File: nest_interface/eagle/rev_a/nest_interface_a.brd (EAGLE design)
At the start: 133.3 x 110.5 mm, 111 parts, among them J1 MOLEX_MICRO_USB_B_047346, J10 CONN_BLOCK_2, J11 CONN_BLOCK_2, J12 CONN_BLOCK_2, J13 CONN_BLOCK_2, J14 CONN_BLOCK_3, J15 CONN_BLOCK_3, J16 CONN_BLOCK_7, J17 CONN_BLOCK_7, J18 CONN_BLOCK_8, J19 CONN_BLOCK_8, J2 MOLEX_MICRO_USB_B_047346, J20 CONN_BLOCK_8, J21 CONN_BLOCK_8, J5 PJ-036A-SMT, J6 CONN_BLOCK_2, J7 CONN_BLOCK_2, J8 CONN_BLOCK_2, J9 CONN_BLOCK_2, U1 EPIC-CORE_A, U2 MSP430F1611IPM, U3 FT232RL, U4 FT232RL, U5 MPC1825, U6 TC1262, U7 PCA9575, U8 PCA9575, Y1 FC-135_32.768KA-A3

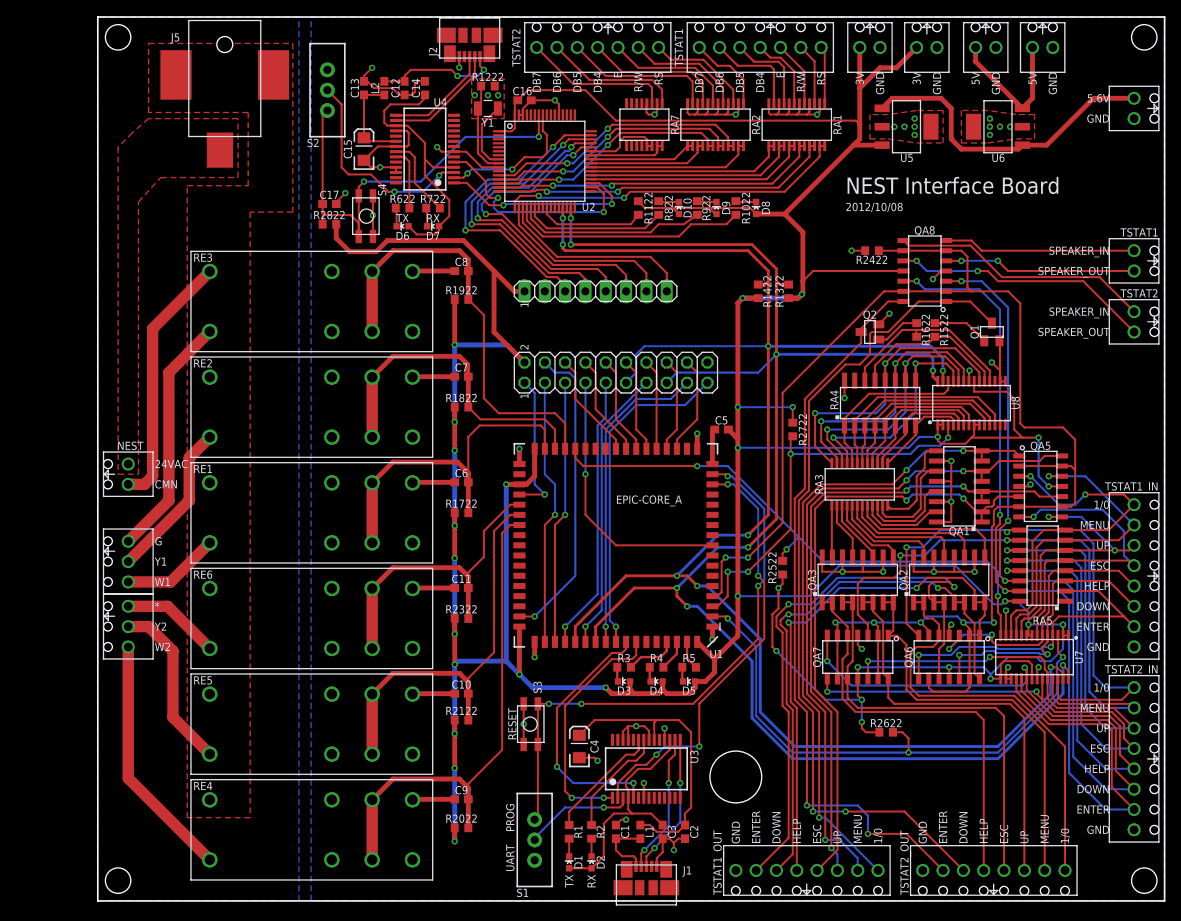
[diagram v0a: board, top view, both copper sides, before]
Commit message: added decoupling caps, bom
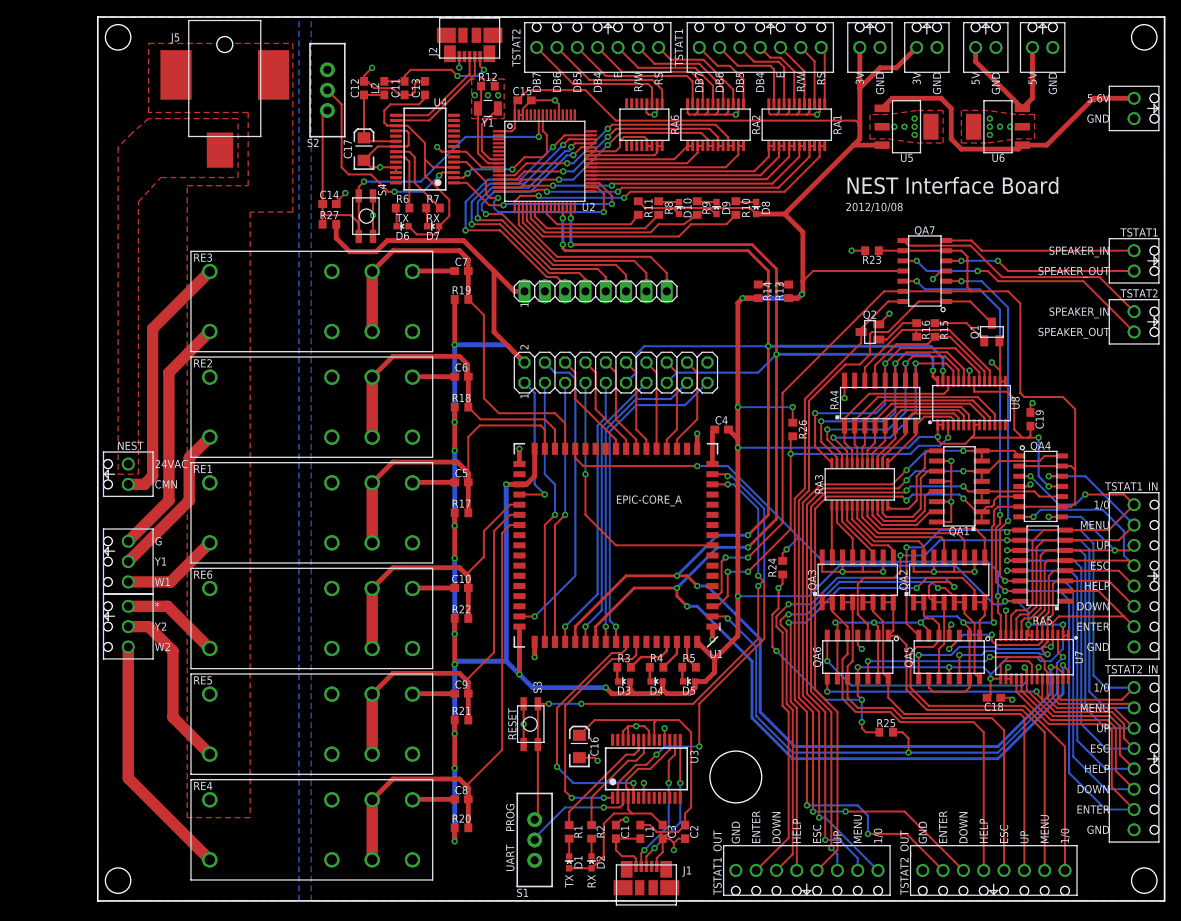
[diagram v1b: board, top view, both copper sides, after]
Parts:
- removed QA8: ALD1107, nest_interface:SOIC-14
- added C18, C19: 0.1u, rcl:C0603
- added QA4: ALD1107, nest_interface:SOIC-14
- C10, C11, C6, C7, C8, C9: value .1u -> 0.1u
- C15: value 10u -> 1u; device SparkFun:EIA3216 -> rcl:C0603
- C16: value 1u -> 10u; device rcl:C0603 -> SparkFun:EIA3216
- C17: value 0.1u -> 10u; device rcl:C0603 -> SparkFun:EIA3216
- C4: value 10u -> 0.1u; device SparkFun:EIA3216 -> rcl:C0603
- moved C16 81.1 mm to (60.2, 19.3), turned to 90 degrees
- moved C8 66.0 mm to (45.5, 12.7)
- moved C11 62.9 mm to (38.4, 101.6), turned to 270 degrees
- moved QA7 49.0 mm to (103.4, 78.7), turned to 90 degrees
- moved C4 43.4 mm to (78.0, 58.9), turned to 180 degrees
- moved C5 33.2 mm to (45.5, 52.3)
- moved QA5 24.2 mm to (106.4, 30.5), turned to 180 degrees
- moved C15 21.0 mm to (53.3, 100.1), turned to 0 degrees
- moved C14 18.8 mm to (29.0, 87.1), turned to 0 degrees
- moved C9 13.2 mm to (45.5, 25.9)
- moved C10 13.2 mm to (45.5, 39.1)
- moved C6 13.2 mm to (45.5, 65.5)
- moved C7 13.2 mm to (45.5, 78.7)
- moved QA6 11.4 mm to (95.0, 30.5)
- moved C17 8.10 mm to (33.3, 94.0), turned to 90 degrees
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- renumbered JP1 to J4, R1022 to R10, R1122 to R11, R1222 to R12, R1322 to R13, R1422 to R14, R1522 to R15, R1622 to R16, R1722 to R17, R1822 to R18, R1922 to R19, R2022 to R20, R2122 to R21, R2322 to R22, R2422 to R23, R2522 to R24, R2622 to R25, R2722 to R26, R2822 to R27, R622 to R6, R722 to R7, R822 to R8, R922 to R9, RA7 to RA6
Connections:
- net #KEYPAD_ENABLE: now also QA4.13, QA4.2, QA4.6, QA4.9; no longer QA8.13, QA8.2, QA8.6, QA8.9
- net COOLING1_PIN: now also C6.1; no longer C7.1
- net COOLING2_PIN: now also C9.1; no longer C10.1
- net FAN_PIN: now also C7.1; no longer C8.1
- net GND: now also C15.2, C16.C, C17.C, C18.2, C19.2, C5.2, QA4.4; no longer C15.C, C16.2, C17.2, C4.C, QA8.4
- net HEATING1_PIN: now also C5.1; no longer C6.1
- net HEATING2_PIN: now also C8.1; no longer C9.1
- net N$18: now also C4.2; no longer C5.2
- net N$39: now also C11.1; no longer C12.1
- net N$43: now also C12.1, C17.A; no longer C13.1, C15.A
- net N$51: now also C13.1; no longer C14.1
- net N$6: now also C16.A; no longer C4.A
- net RST1: now also C14.1; no longer C17.1
- net STAR_PIN: now also C10.1; no longer C11.1
- net TSTAT1_DOWN_IN: now also QA5.12; no longer QA6.12
- net TSTAT1_DOWN_OUT: now also QA5.14; no longer QA6.14
- net TSTAT1_ENTER_IN: now also QA5.8; no longer QA6.8
- net TSTAT1_ENTER_OUT: now also QA5.10; no longer QA6.10
- net TSTAT1_ESC_IN: now also QA4.7; no longer QA5.7
- net TSTAT1_ESC_OUT: now also QA4.5; no longer QA5.5
- net TSTAT1_HELP_IN: now also QA5.3; no longer QA6.3
- net TSTAT1_HELP_OUT: now also QA5.1; no longer QA6.1
- net TSTAT1_MENU_IN: now also QA4.12; no longer QA5.12
- net TSTAT1_MENU_OUT: now also QA4.14; no longer QA5.14
- net TSTAT1_ON/OFF_IN: now also QA4.3; no longer QA5.3
- net TSTAT1_ON/OFF_OUT: now also QA4.1; no longer QA5.1
- net TSTAT1_SPEAKER_IN: now also QA7.7; no longer QA8.7
- net TSTAT1_SPEAKER_OUT: now also QA7.5; no longer QA8.5
- net TSTAT1_UP_IN: now also QA4.8; no longer QA5.8
- net TSTAT1_UP_OUT: now also QA4.10; no longer QA5.10
- net TSTAT2_DOWN_IN: now also QA7.3; no longer QA8.3
- net TSTAT2_DOWN_OUT: now also QA7.1; no longer QA8.1
- net TSTAT2_ENTER_IN: now also QA7.12; no longer QA8.12
- net TSTAT2_ENTER_OUT: now also QA7.14; no longer QA8.14
- net TSTAT2_ESC_IN: now also QA6.8; no longer QA7.8
- net TSTAT2_ESC_OUT: now also QA6.10; no longer QA7.10
- net TSTAT2_HELP_IN: now also QA6.7; no longer QA7.7
- net TSTAT2_HELP_OUT: now also QA6.5; no longer QA7.5
- net TSTAT2_MENU_IN: now also QA6.3; no longer QA7.3
- net TSTAT2_MENU_OUT: now also QA6.1; no longer QA7.1
- net TSTAT2_ON/OFF_IN: now also QA5.7; no longer QA6.7
- net TSTAT2_ON/OFF_OUT: now also QA5.5; no longer QA6.5
- net TSTAT2_SPEAKER_IN: now also QA7.8; no longer QA8.8
- net TSTAT2_SPEAKER_OUT: now also QA7.10; no longer QA8.10
- net TSTAT2_UP_IN: now also QA6.12; no longer QA7.12
- net TSTAT2_UP_OUT: now also QA6.14; no longer QA7.14
- net VCC: now also C15.1, C18.1, C19.1, C4.1, QA4.11; no longer C16.1, C5.1, QA8.11
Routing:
- net VCC: track 602.7 -> 606.8 mm
- net GND: track 224.8 -> 227.6 mm, vias 52 -> 54
- net TSTAT2_ESC_OUT: track 53.3 -> 52.2 mm
- net TSTAT2_HELP_OUT: track 51.9 -> 51.0 mm

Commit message: added board for keypad socket
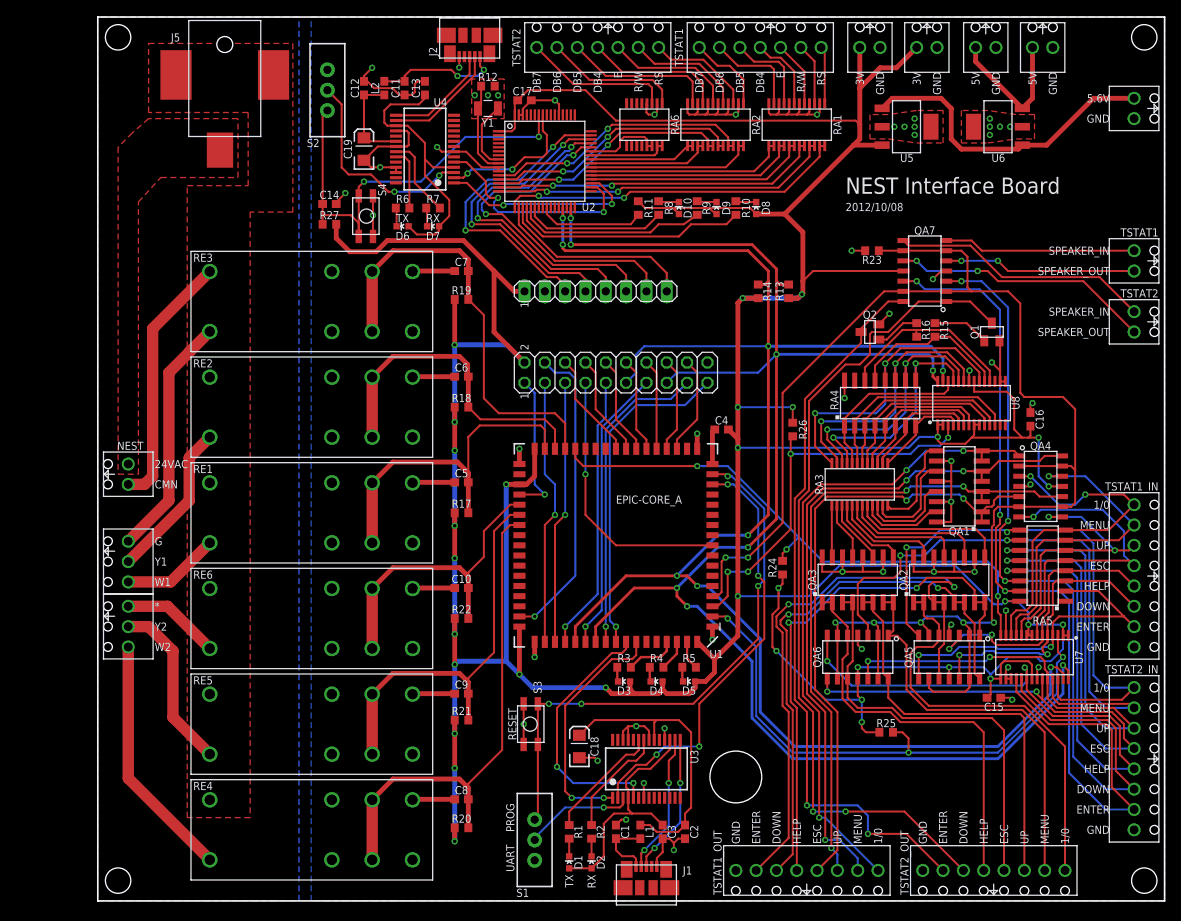
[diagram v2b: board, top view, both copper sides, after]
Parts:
- C15: value 1u -> 0.1u
- C16: value 10u -> 0.1u; device SparkFun:EIA3216 -> rcl:C0603
- C17: value 10u -> 1u; device SparkFun:EIA3216 -> rcl:C0603
- C18, C19: value 0.1u -> 10u; device rcl:C0603 -> SparkFun:EIA3216
- D1, D3, D6, D8: value (none) -> RED
- D10, D2, D5, D7: value (none) -> BLUE
- D4, D9: value (none) -> GREEN
- moved C15 95.0 mm to (112.0, 25.4)
- moved C19 89.9 mm to (33.3, 94.0)
- moved C16 69.7 mm to (116.6, 60.2)
- moved C18 52.2 mm to (60.2, 19.3), turned to 90 degrees
- moved C17 21.0 mm to (53.3, 100.1), turned to 0 degrees
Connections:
- net GND: now also C16.2, C17.2, C18.C, C19.C; no longer C16.C, C17.C, C18.2, C19.2
- net N$43: now also C19.A; no longer C17.A
- net N$6: now also C18.A; no longer C16.A
- net VCC: now also C16.1, C17.1; no longer C18.1, C19.1

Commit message: nest
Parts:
- removed J4: (no value), pinhead:1X08
- added JP1: (no value), pinhead:1X10
- added U$1: UMICH_SOLID_LARGE, nest_interface:UMICH_SOLID_350MIL
- moved S2 2.40 mm to (30.7, 102.6)
- moved C11 1.61 mm to (39.9, 102.1)
- moved C12 1.61 mm to (34.8, 102.1)
- moved C13 1.61 mm to (42.4, 102.1)
- moved L2 1.61 mm to (37.3, 102.1)
- moved C19 0.51 mm to (33.8, 94.0)
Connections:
- net P2.3 renamed LCDP_P2.3
- removed net P5.4: U2.48
- new net LCDP_P5.4: JP1.2, U2.48
- net GND: now also JP1.10; no longer J4.2
- net LCDP_MISO1: now also JP1.5; no longer J4.4
- net LCDP_MOSI1: now also JP1.6; no longer J4.5
- net LCDP_P1.6: now also JP1.8; no longer J4.7
- net LCDP_P1.7: now also JP1.9; no longer J4.8
- net LCDP_P2.4: now also JP1.3
- net LCDP_STE1: now also JP1.7; no longer J4.6
- net LCDP_UCLK1: now also JP1.4; no longer J4.3
- net VCC: now also JP1.1; no longer J4.1
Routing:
- net LCDP_P5.4: track 0.00 -> 39.8 mm, vias 0 -> 2
- net LCDP_P2.4: track 0.00 -> 13.7 mm, vias 0 -> 2
- net LCDP_MISO1: track 39.6 -> 43.8 mm
- net LCDP_MOSI1: track 40.2 -> 44.3 mm
- net LCDP_STE1: track 40.8 -> 44.7 mm
- net LCDP_P1.6: track 22.9 -> 26.6 mm
- net LCDP_P1.7: track 24.8 -> 28.5 mm
- net LCDP_UCLK1: track 38.8 -> 42.4 mm
- net N$51: track 35.0 -> 37.2 mm
- net RST1: track 55.2 -> 57.3 mm
- net N$39: track 15.9 -> 14.2 mm
- net GND: track 227.6 -> 226.6 mm
- net VCC: track 606.8 -> 607.6 mm
- net N$43: track 12.1 -> 12.8 mm
- net #KEYPAD_ENABLE: track 197.0 -> 196.2 mm
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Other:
- board text added: "24VAC SIGNALS"
- board text added: "LCD"
- board text added: "MAIN CONTROLLER"
- board text added: "VCC"

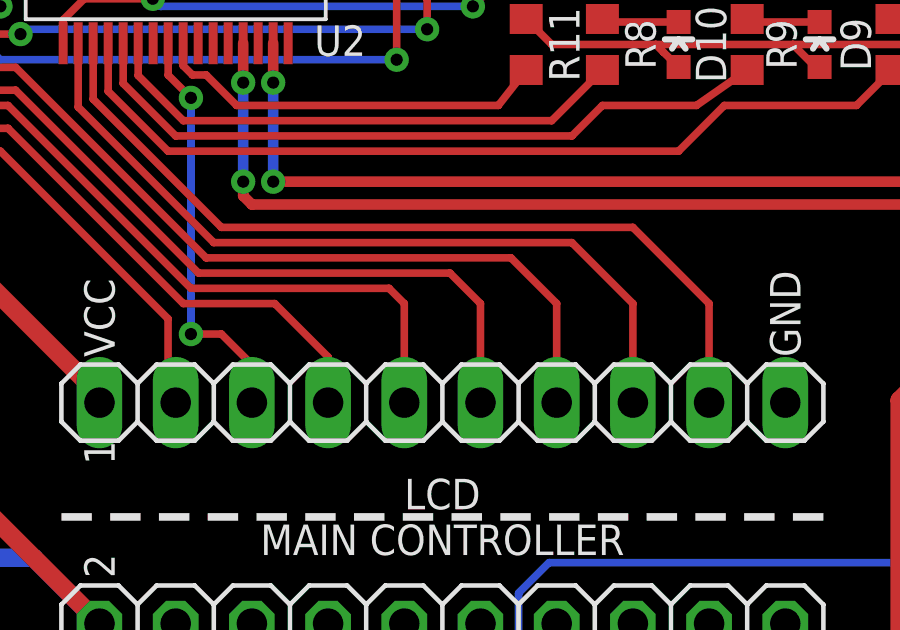
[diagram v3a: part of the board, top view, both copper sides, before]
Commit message: cleaned up two traces and started lcd code
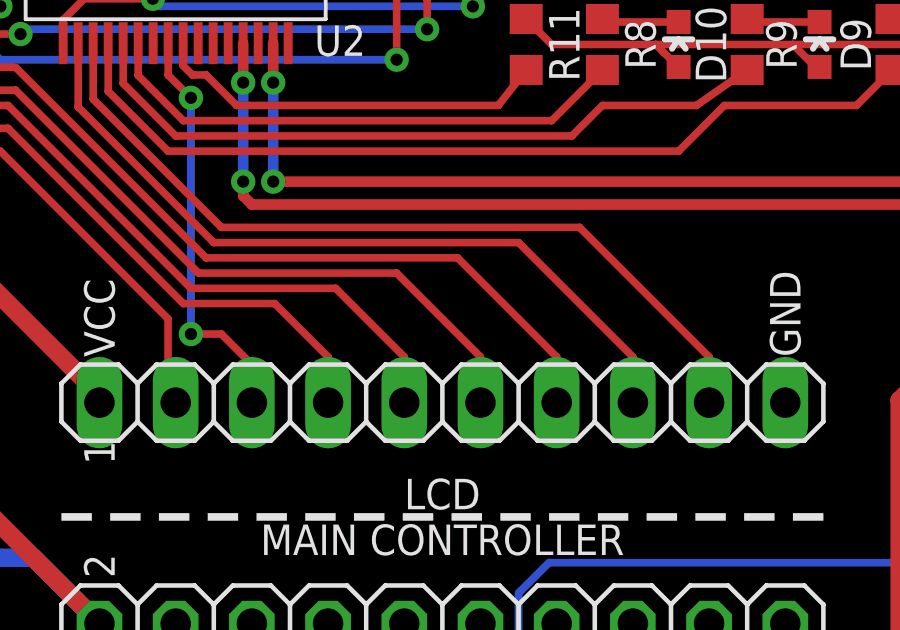
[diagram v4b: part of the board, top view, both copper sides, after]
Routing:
- net LCDP_P1.7: track 28.5 -> 27.5 mm
- net LCDP_MOSI1: track 44.3 -> 43.3 mm
- net LCDP_MISO1: track 43.8 -> 42.7 mm
- net LCDP_STE1: track 44.7 -> 43.7 mm
- net LCDP_P1.6: track 26.6 -> 25.6 mm
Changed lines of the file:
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@@
 <wire x1="50.546" y1="85.852" x2="56.896" y2="79.502" width="0.254" layer="1"/>
 <contactref element="JP1" pad="7"/>
-<wire x1="56.896" y1="79.502" x2="67.056" y2="79.502" width="0.254" layer="1"/>
-<wire x1="67.056" y1="79.502" x2="68.58" y2="77.978" width="0.254" layer="1"/>
-<wire x1="68.58" y1="77.978" x2="68.58" y2="74.676" width="0.254" layer="1"/>
+<wire x1="56.896" y1="79.502" x2="65.278" y2="79.502" width="0.254" layer="1"/>
+<wire x1="65.278" y1="79.502" x2="68.58" y2="76.2" width="0.254" layer="1"/>
+<wire x1="68.58" y1="76.2" x2="68.58" y2="74.676" width="0.254" layer="1"/>
 </signal>
 <signal name="LCDP_MOSI1">
@@
 <wire x1="59.182" y1="93.98" x2="59.182" y2="94.234" width="0.254" layer="16"/>
 <contactref element="JP1" pad="6"/>
-<wire x1="56.642" y1="78.994" x2="65.024" y2="78.994" width="0.254" layer="1"/>
-<wire x1="65.024" y1="78.994" x2="66.04" y2="77.978" width="0.254" layer="1"/>
-<wire x1="66.04" y1="77.978" x2="66.04" y2="74.676" width="0.254" layer="1"/>
+<wire x1="56.642" y1="78.994" x2="63.246" y2="78.994" width="0.254" layer="1"/>
+<wire x1="63.246" y1="78.994" x2="66.04" y2="76.2" width="0.254" layer="1"/>
+<wire x1="66.04" y1="76.2" x2="66.04" y2="74.676" width="0.254" layer="1"/>
 </signal>
 <signal name="LCDP_MISO1">
@@
 <wire x1="50.292" y1="84.582" x2="56.388" y2="78.486" width="0.254" layer="1"/>
 <contactref element="JP1" pad="5"/>
-<wire x1="56.388" y1="78.486" x2="62.992" y2="78.486" width="0.254" layer="1"/>
-<wire x1="62.992" y1="78.486" x2="63.5" y2="77.978" width="0.254" layer="1"/>
-<wire x1="63.5" y1="77.978" x2="63.5" y2="74.676" width="0.254" layer="1"/>
+<wire x1="56.388" y1="78.486" x2="61.214" y2="78.486" width="0.254" layer="1"/>
+<wire x1="61.214" y1="78.486" x2="63.5" y2="76.2" width="0.254" layer="1"/>
+<wire x1="63.5" y1="76.2" x2="63.5" y2="74.676" width="0.254" layer="1"/>
 </signal>
 <signal name="LCDP_UCLK1">
@@
 <wire x1="52.63" y1="84.53" x2="57.15" y2="80.01" width="0.254" layer="1"/>
 <contactref element="JP1" pad="8"/>
-<wire x1="57.15" y1="80.01" x2="69.088" y2="80.01" width="0.254" layer="1"/>
-<wire x1="69.088" y1="80.01" x2="71.12" y2="77.978" width="0.254" layer="1"/>
-<wire x1="71.12" y1="77.978" x2="71.12" y2="74.676" width="0.254" layer="1"/>
+<wire x1="57.15" y1="80.01" x2="67.31" y2="80.01" width="0.254" layer="1"/>
+<wire x1="67.31" y1="80.01" x2="71.12" y2="76.2" width="0.254" layer="1"/>
+<wire x1="71.12" y1="76.2" x2="71.12" y2="74.676" width="0.254" layer="1"/>
 </signal>
 <signal name="LCDP_P1.7">
@@
 <wire x1="53.13" y1="84.792" x2="57.404" y2="80.518" width="0.254" layer="1"/>
 <contactref element="JP1" pad="9"/>
-<wire x1="57.404" y1="80.518" x2="71.12" y2="80.518" width="0.254" layer="1"/>
-<wire x1="71.12" y1="80.518" x2="73.66" y2="77.978" width="0.254" layer="1"/>
-<wire x1="73.66" y1="77.978" x2="73.66" y2="74.676" width="0.254" layer="1"/>
+<wire x1="57.404" y1="80.518" x2="69.342" y2="80.518" width="0.254" layer="1"/>
+<wire x1="69.342" y1="80.518" x2="73.66" y2="76.2" width="0.254" layer="1"/>
+<wire x1="73.66" y1="76.2" x2="73.66" y2="74.676" width="0.254" layer="1"/>
 </signal>
 <signal name="LCDP_P2.3">
